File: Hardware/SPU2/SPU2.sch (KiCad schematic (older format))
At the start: 13 parts

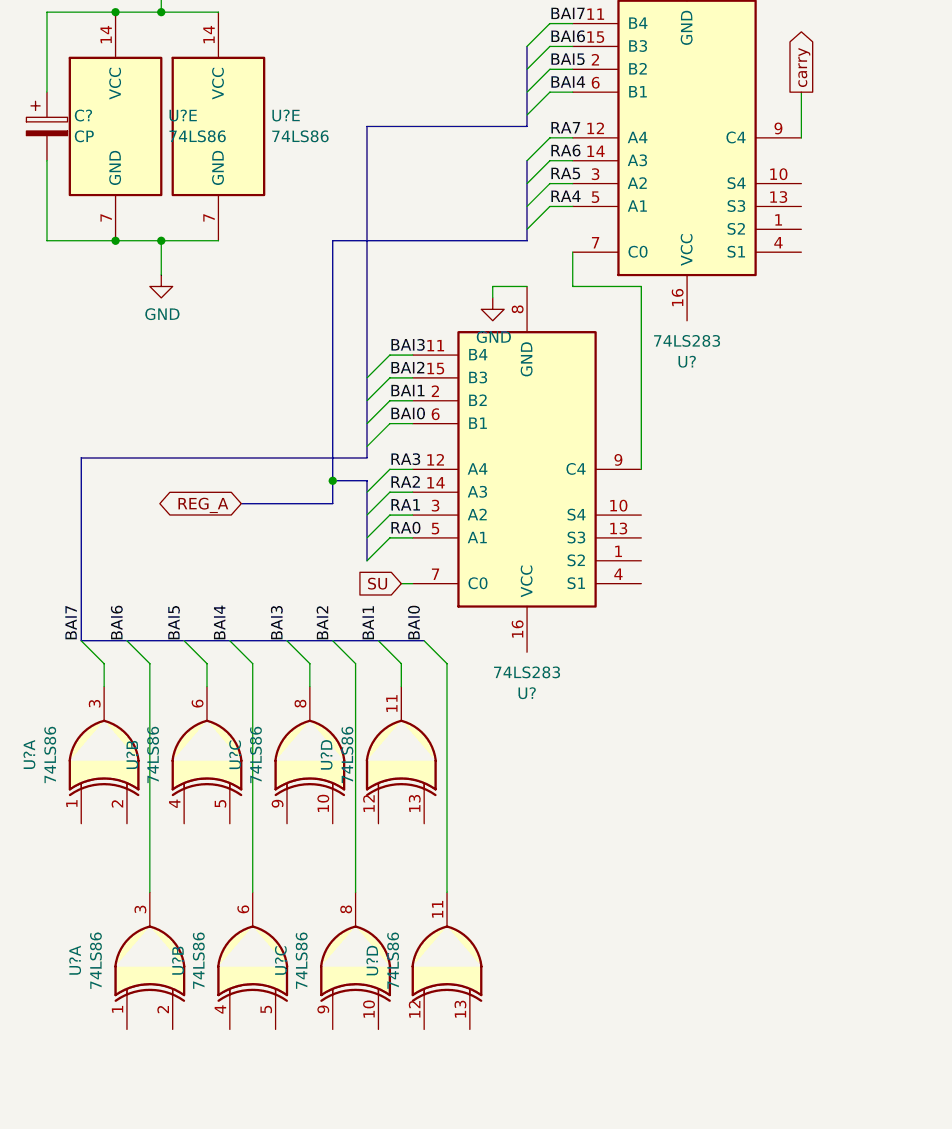
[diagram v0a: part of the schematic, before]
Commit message: finished ALU arithmetic
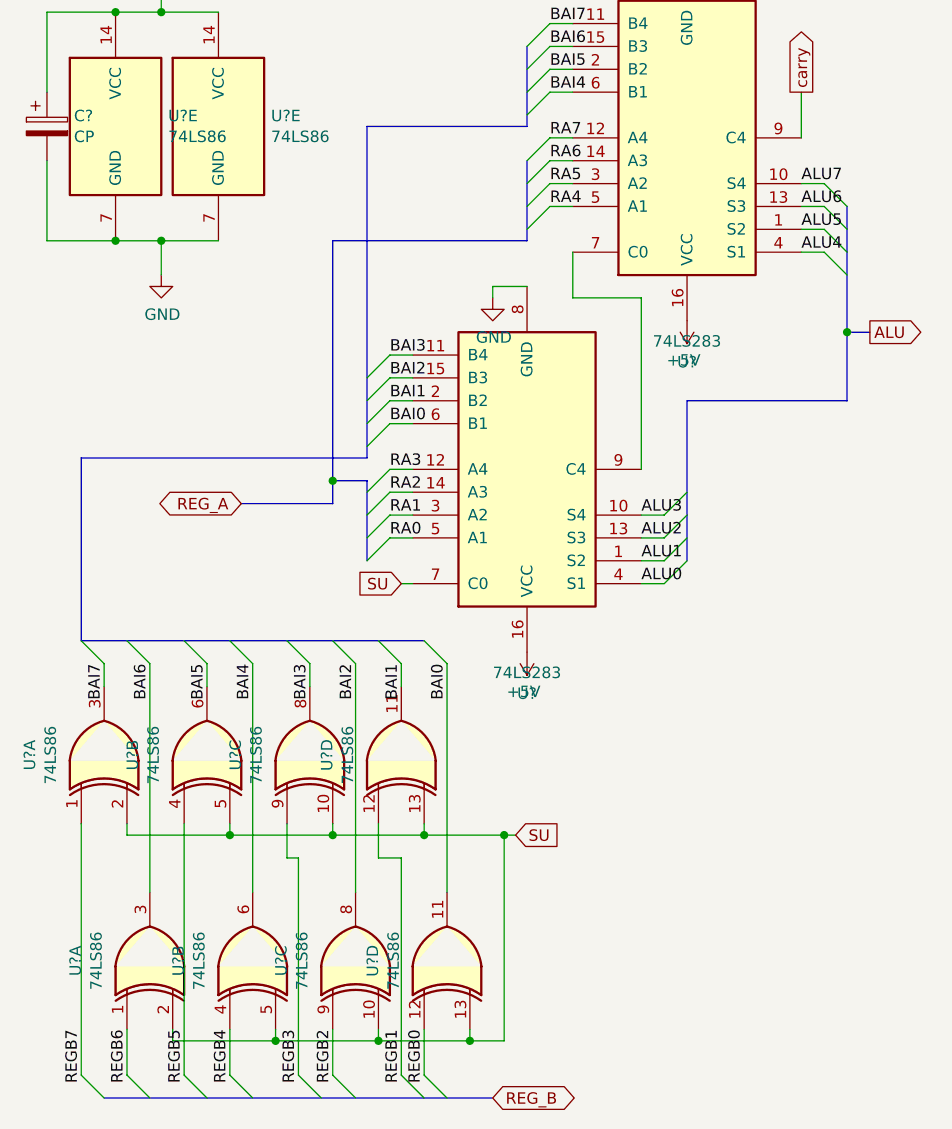
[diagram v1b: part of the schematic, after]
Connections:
- net +5V: now also U?.16 (VCC), U?.16 (VCC)
- net BAI0: now also U?.11
- net BAI1: now also U?.11
- net BAI2: now also U?.8
- net BAI3: now also U?.8
- net BAI4: now also U?.6
- net BAI5: now also U?.6
- net BAI6: now also U?.3
- net BAI7: now also U?.3
- net SU: now also U?.10, U?.10, U?.13, U?.13, U?.2, U?.2, U?.5, U?.5
- net ALU1: now reaches U?.1 (S2)
- net ALU3: now reaches U?.10 (S4)
- net ALU2: now reaches U?.13 (S3)
- net ALU0: now reaches U?.4 (S1)
- net ALU5: now reaches U?.1 (S2)
- net ALU7: now reaches U?.10 (S4)
- net ALU6: now reaches U?.13 (S3)
- net ALU4: now reaches U?.4 (S1)
- net REGB7: now reaches U?.1
- net REGB5: now reaches U?.4
- net REGB3: now reaches U?.9
- net REGB1: now reaches U?.12
- net REGB6: now reaches U?.1
- net REGB4: now reaches U?.4
- net REGB2: now reaches U?.9
- net REGB0: now reaches U?.12
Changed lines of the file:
@@
 EESchema Schematic File Version 4
+LIBS:SPU2-cache
 EELAYER 30 0
 EELAYER END
@@
 	2250 3350 2300 3350
 Wire Wire Line
-	3300 2050 3000 2050
-Wire Wire Line
-	3000 1900 3000 2050
+	3300 2100 3000 2100
+Wire Wire Line
+	3000 1900 3000 2100
 Wire Bus Line
 	1950 3000 1550 3000
@@
 Wire Wire Line
 	2250 3800 2250 3700
-Text Label 2350 3600 1    50   ~ 0
+Text Label 2450 3700 3    50   ~ 0
 BAI0
-Text Label 2150 3600 1    50   ~ 0
+Text Label 2250 3700 3    50   ~ 0
 BAI1
-Text Label 1950 3600 1    50   ~ 0
+Text Label 2050 3700 3    50   ~ 0
 BAI2
-Text Label 1750 3600 1    50   ~ 0
+Text Label 1850 3700 3    50   ~ 0
 BAI3
-Text Label 1500 3600 1    50   ~ 0
+Text Label 1600 3700 3    50   ~ 0
 BAI4
-Text Label 1300 3600 1    50   ~ 0
+Text Label 1400 3700 3    50   ~ 0
 BAI5
-Text Label 1050 3600 1    50   ~ 0
+Text Label 1150 3700 3    50   ~ 0
 BAI6
-Text Label 850  3600 1    50   ~ 0
+Text Label 950  3700 3    50   ~ 0
 BAI7
 Entry Wire Line
@@
 RA7
 Wire Wire Line
-	3300 2050 3300 2850
+	3300 2100 3300 2850
 $Comp
 L power:GND #PWR?
@@
 Wire Bus Line
 	850  2800 850  3600
+Wire Wire Line
+	3400 3050 3300 3050
+Wire Wire Line
+	3400 3150 3300 3150
+Wire Wire Line
+	3400 3250 3300 3250
+Wire Wire Line
+	3400 3350 3300 3350
+Wire Wire Line
+	4100 1600 4000 1600
+Wire Wire Line
+	4100 1700 4000 1700
+Wire Wire Line
+	4100 1800 4000 1800
+Wire Wire Line
+	4100 1900 4000 1900
+Entry Wire Line
+	4100 1600 4200 1700
+Entry Wire Line
+	4100 1700 4200 1800
+Entry Wire Line
+	4100 1800 4200 1900
+Entry Wire Line
+	4100 1900 4200 2000
+Entry Wire Line
+	3400 3350 3500 3250
+Entry Wire Line
+	3400 3250 3500 3150
+Entry Wire Line
+	3400 3150 3500 3050
+Entry Wire Line
+	3400 3050 3500 2950
+$Comp
+L power:+5V #PWR?
+U 1 1 5EC1C29E
+P 2800 3650
+F 0 "#PWR?" H 2800 3500 50  0001 C CNN
+F 1 "+5V" H 2815 3823 50  0000 C CNN
+F 2 "" H 2800 3650 50  0001 C CNN
+F 3 "" H 2800 3650 50  0001 C CNN
+	1    2800 3650
+	-1   0    0    1
+$EndComp
+$Comp
+L power:+5V #PWR?
+U 1 1 5EC1F243
+P 3500 2200
+F 0 "#PWR?" H 3500 2050 50  0001 C CNN
+F 1 "+5V" H 3515 2373 50  0000 C CNN
+F 2 "" H 3500 2200 50  0001 C CNN
+F 3 "" H 3500 2200 50  0001 C CNN
+	1    3500 2200
+	-1   0    0    1
+$EndComp
+Text Label 3300 3350 0    50   ~ 0
+ALU0
+Text Label 3300 3250 0    50   ~ 0
+ALU1
+Text Label 3300 3150 0    50   ~ 0
+ALU2
+Text Label 3300 3050 0    50   ~ 0
+ALU3
+Text Label 4000 1900 0    50   ~ 0
+ALU4
+Text Label 4000 1800 0    50   ~ 0
+ALU5
+Text Label 4000 1700 0    50   ~ 0
+ALU6
+Text Label 4000 1600 0    50   ~ 0
+ALU7
+Wire Bus Line
+	3500 2550 4200 2550
+Text GLabel 4300 2250 2    50   Output ~ 0
+ALU
+Wire Bus Line
+	4300 2250 4200 2250
+Connection ~ 4200 2250
+Wire Bus Line
+	4200 2250 4200 2550
+Wire Wire Line
+	850  4400 850  5500
+Wire Wire Line
+	1050 5300 1050 5500
+Wire Wire Line
+	1300 4400 1300 5500
+Wire Wire Line
+	1500 5300 1500 5500
+Wire Wire Line
+	1950 5300 1950 5500
+Wire Wire Line
+	2350 5300 2350 5500
+Wire Wire Line
+	2150 4400 2150 4550
+Wire Wire Line
+	2150 4550 2250 4550
+Wire Wire Line
+	2250 4550 2250 5500
+Wire Wire Line
+	1750 4400 1750 4550
+Wire Wire Line
+	1750 4550 1800 4550
+Wire Wire Line
+	1800 4550 1800 5500
+Entry Wire Line
+	2350 5500 2450 5600
+Entry Wire Line
+	2250 5500 2350 5600
+Entry Wire Line
+	1950 5500 2050 5600
+Entry Wire Line
+	1800 5500 1900 5600
+Entry Wire Line
+	1500 5500 1600 5600
+Entry Wire Line
+	1300 5500 1400 5600
+Entry Wire Line
+	1050 5500 1150 5600
+Entry Wire Line
+	850  5500 950  5600
+Text Label 2350 5300 3    50   ~ 0
+REGB0
+Text Label 2250 5300 3    50   ~ 0
+REGB1
+Text Label 1950 5300 3    50   ~ 0
+REGB2
+Text Label 1800 5300 3    50   ~ 0
+REGB3
+Text Label 1500 5300 3    50   ~ 0
+REGB4
+Text Label 1300 5300 3    50   ~ 0
+REGB5
+Text Label 1050 5300 3    50   ~ 0
+REGB6
+Text Label 850  5300 3    50   ~ 0
+REGB7
+Text GLabel 2650 5600 2    50   BiDi ~ 0
+REG_B
+Wire Wire Line
+	1050 4450 1500 4450
+Wire Wire Line
+	1500 4450 1500 4400
+Wire Wire Line
+	1050 4450 1050 4400
+Wire Wire Line
+	1500 4450 1950 4450
+Wire Wire Line
+	1950 4450 1950 4400
+Connection ~ 1500 4450
+Wire Wire Line
+	1950 4450 2350 4450
+Wire Wire Line
+	2350 4450 2350 4400
+Connection ~ 1950 4450
+Wire Wire Line
+	1250 5300 1250 5350
+Wire Wire Line
+	1250 5350 1700 5350
+Wire Wire Line
+	1700 5350 1700 5300
+Wire Wire Line
+	1700 5350 2150 5350
+Wire Wire Line
+	2150 5350 2150 5300
+Connection ~ 1700 5350
+Wire Wire Line
+	2150 5350 2550 5350
+Wire Wire Line
+	2550 5350 2550 5300
+Connection ~ 2150 5350
+Wire Wire Line
+	2350 4450 2700 4450
+Wire Wire Line
+	2700 4450 2700 5350
+Wire Wire Line
+	2700 5350 2550 5350
+Connection ~ 2350 4450
+Connection ~ 2550 5350
+Text GLabel 2750 4450 2    50   Input ~ 0
+SU
+Wire Wire Line
+	2750 4450 2700 4450
+Wire Bus Line
+	3500 2550 3500 3250
+Wire Bus Line
+	4200 1700 4200 2250
 Wire Bus Line
 	2100 2900 2100 3250
@@
 Wire Bus Line
 	2100 1350 2100 2800
+Wire Bus Line
+	950  5600 2650 5600
+Connection ~ 2700 4450
 $EndSCHEMATC

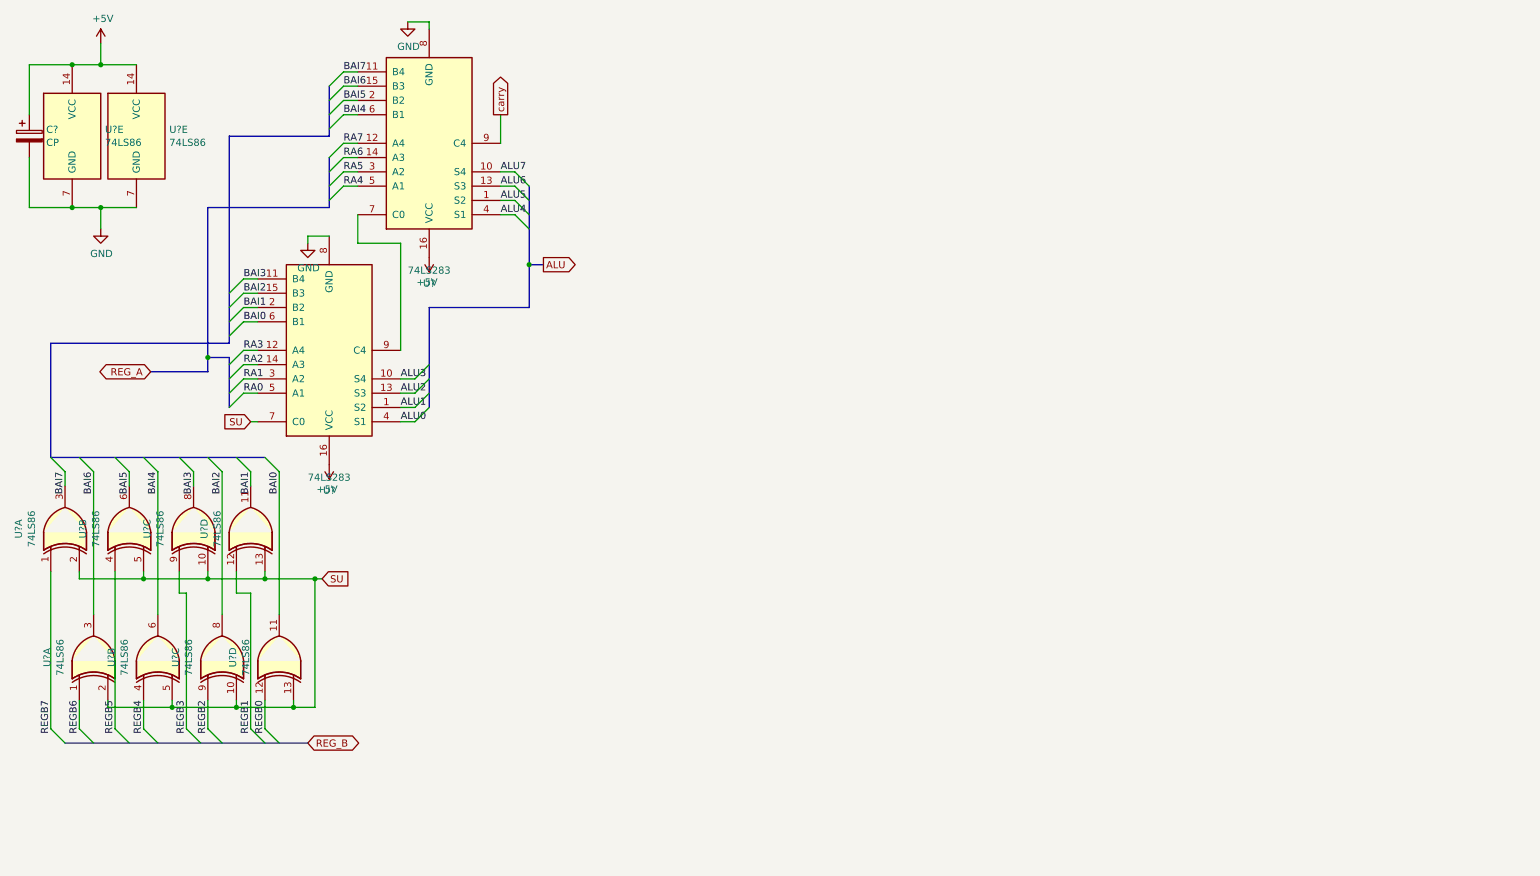
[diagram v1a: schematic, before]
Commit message: finished zero and equal flags
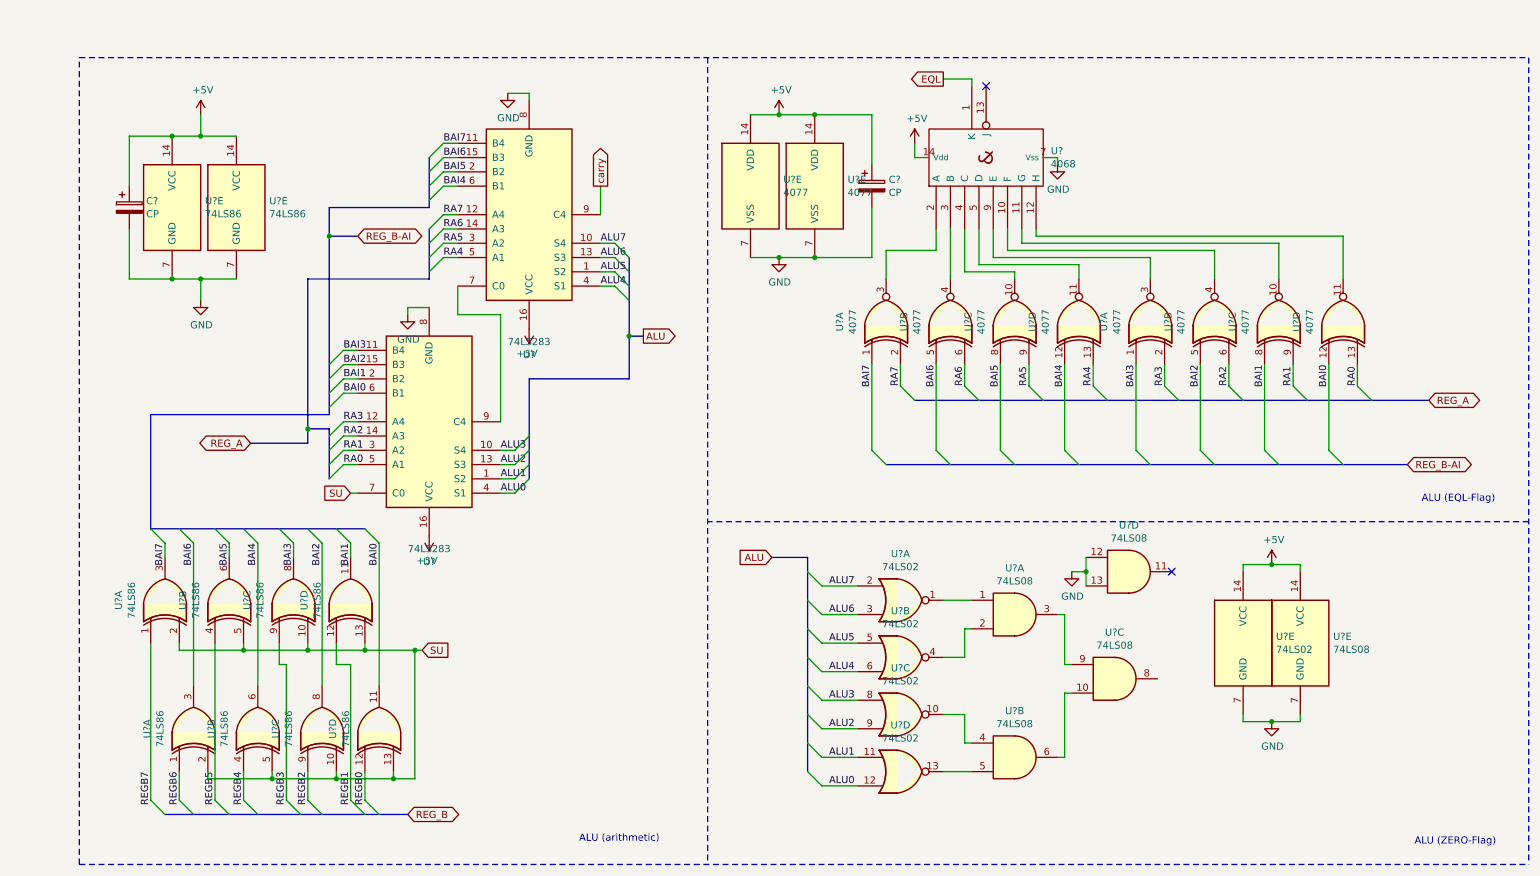
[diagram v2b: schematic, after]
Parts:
- added C?: CP, symbol Device:CP
- added U?: 4068, symbol 4xxx_IEEE_:4068
- added U? (x10): 4077, symbol 4xxx:4077
- added U? (x5): 74LS02, symbol 74xx:74LS02
- added U? (x5): 74LS08, symbol 74xx:74LS08
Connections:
- net +5V: now also C?.1, U?.14 (VCC), U?.14 (VCC), U?.14 (VDD), U?.14 (VDD), U?.14 (Vdd)
- net ALU0: now also U?.12
- net ALU1: now also U?.11
- net ALU2: now also U?.9
- net ALU3: now also U?.8
- net ALU4: now also U?.6
- net ALU5: now also U?.5
- net ALU6: now also U?.3
- net ALU7: now also U?.2
- net BAI0: now also U?.12
- net BAI1: now also U?.8
- net BAI2: now also U?.5
- net BAI3: now also U?.1
- net BAI4: now also U?.12
- net BAI5: now also U?.8
- net BAI6: now also U?.5
- net BAI7: now also U?.1
- net GND: now also C?.2, U?.12, U?.13, U?.7 (GND), U?.7 (GND), U?.7 (VSS), U?.7 (VSS), U?.7 (Vss)
- net RA0: now also U?.13
- net RA1: now also U?.9
- net RA2: now also U?.6
- net RA3: now also U?.2
- net RA4: now also U?.13
- net RA5: now also U?.9
- net RA6: now also U?.6
- net RA7: now also U?.2
- new net: U?.10 (F), U?.4
- new net: U?.10, U?.11 (G)
- new net: U?.11, U?.12 (H)
- new net: U?.2 (A), U?.3
- new net: U?.3 (B), U?.4
- new net: U?.10, U?.4 (C)
- new net: U?.11, U?.5 (D)
- new net: U?.3, U?.9 (E)
- new net: U?.1, U?.1
- new net: U?.2, U?.4
- new net: U?.10, U?.4
- new net: U?.13, U?.5
- new net: U?.3, U?.9
- new net: U?.10, U?.6
- new net EQL: U?.1 (K)
- no-connect marks 0 -> 2
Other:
- note added: "ALU (EQL-Flag)\n\n"
- note added: "ALU (ZERO-Flag)\n\n"
- note added: "ALU (arithmetic)\n"
- moved on the sheet: C?, U?, U?A, U?B, U?C, U?D, U?E

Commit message: ich geh jz pennen gn :)
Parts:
- added D1, D2, D3, D4, D5, D6, D7, D8, D? (x8): LED, symbol Device:LED
- added R1, R2, R3, R4, R5, R6, R7, R8, R? (x8): R, symbol Device:R
- added U11, U12, U? (x2): 74LS173, symbol 74xx:74LS173
- added U13, U3, U?: 74LS245, symbol 74xx:74LS245
- gave numbers to parts that had none: 11
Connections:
- net labels added: CLK, D0, D1, D2, D3, D4, D5, D6, D7, DATA, ZERO, ~AI, ~AO, ~BI, ~BO, ~EO
- wire segments 166 -> 362
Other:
- note added: "ALU (LEDs)\n"
- note added: "ALU (output control)"
- note added: "REGISTER A\n"
- note added: "REGISTER B\n\n"
- moved on the sheet: U10A, U10B, U10C, U10D, U10E, U8A, U8B, U8C, U8D, U8E

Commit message: random push
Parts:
- removed U13, U?: 74LS245, symbol 74xx:74LS245
- added C? (x4): CP, symbol Device:CP
- added D? (x8): LED, symbol Device:LED
- added R? (x8): R, symbol Device:R
- added U? (x3): 74LS161, symbol 74xx:74LS161
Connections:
- net labels added: CE
- net labels removed: ~AO, ~BO
- wire segments 362 -> 406
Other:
- moved on the sheet: D1, D2, D3, D4, D5, D6, D7, D8, D?, R1, R2, R3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

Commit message: foo
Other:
- note added: "PROGRAM COUNTER"
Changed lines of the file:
@@
 Wire Notes Line
 	1050 6450 11200 6450
-Wire Notes Line
-	11200 800  11200 6450
 Text Notes 10400 6400 0    50   ~ 0
 ALU (ZERO-Flag)\n\n
@@
 Wire Wire Line
 	2050 6800 2050 6850
-Wire Notes Line
-	1050 8950 3250 8950
 Wire Notes Line
 	3250 8950 3250 6450
@@
 Wire Wire Line
 	4400 8000 4350 8000
-Wire Bus Line
-	17650 1150 18350 1150
-Wire Bus Line
-	15600 1250 15600 1700
-Wire Bus Line
-	16800 2100 16800 2550
-Wire Bus Line
-	13400 1150 14100 1150
-Wire Bus Line
-	11350 1200 11350 1650
-Wire Bus Line
-	12550 2050 12550 2500
-Wire Bus Line
-	4050 4750 4050 5650
-Wire Bus Line
-	2950 6900 2950 7750
-Wire Bus Line
-	1200 6850 1200 7750
-Wire Bus Line
-	6600 4750 6600 6250
-Wire Bus Line
-	6900 3200 10500 3200
-Wire Bus Line
-	6700 3650 10350 3650
-Wire Bus Line
-	1650 6100 3350 6100
-Wire Bus Line
-	4200 3050 4200 3750
-Wire Bus Line
-	4900 2200 4900 2750
-Wire Bus Line
-	2800 3400 2800 3750
-Wire Bus Line
-	3500 2000 3500 2350
-Wire Bus Line
-	2800 2050 2800 3300
-Wire Bus Line
-	3500 1500 3500 1850
-Wire Bus Line
-	1550 4100 3050 4100
 $Comp
 L 74xx:74LS245 U3
@@
 	1    0    0    -1
 $EndComp
+Wire Notes Line
+	11200 800  11200 8950
+Wire Notes Line
+	1050 8950 11200 8950
+Wire Bus Line
+	15600 1250 15600 1700
+Wire Bus Line
+	16800 2100 16800 2550
+Wire Bus Line
+	11350 1200 11350 1650
+Wire Bus Line
+	12550 2050 12550 2500
+Wire Bus Line
+	4200 3050 4200 3750
+Wire Bus Line
+	4900 2200 4900 2750
+Wire Bus Line
+	2800 3400 2800 3750
+Wire Bus Line
+	3500 2000 3500 2350
+Wire Bus Line
+	3500 1500 3500 1850
+Wire Bus Line
+	1550 4100 3050 4100
+Wire Bus Line
+	2800 2050 2800 3300
+Wire Bus Line
+	13400 1150 14100 1150
+Wire Bus Line
+	17650 1150 18350 1150
+Wire Bus Line
+	4050 4750 4050 5650
+Wire Bus Line
+	2950 6900 2950 7750
+Wire Bus Line
+	1200 6850 1200 7750
+Wire Bus Line
+	6600 4750 6600 6250
+Wire Bus Line
+	6900 3200 10500 3200
+Wire Bus Line
+	6700 3650 10350 3650
+Wire Bus Line
+	1650 6100 3350 6100
+Text Notes 10400 8850 0    50   ~ 0
+PROGRAM COUNTER
 $EndSCHEMATC
